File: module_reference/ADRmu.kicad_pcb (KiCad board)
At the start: 4 copper layers, 160 x 100 mm, 139 parts, among them J101 Harting 09042326831, J102 10Vf, J103 10Vs, J104 7Vref, J105 Lo, J301 Conn_01x01, J302 Conn_01x01, J303 Conn_01x01, J304 Conn_01x01, J305 Conn_01x01, Q201 BD135, Q301 MMBT3904, U201 ADR1000, U202 OPA2140, U203 ADA4523-1, U301 L78L33_SOT89, U302 LT3439, U303 TMP117, U304 BR24H64FVM, U305 LT3045xMSE

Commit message: Lowered Vreg to 11V to keep things cooler
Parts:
- R311: value 120k -> 110k
- R312: value 1M8 -> 1M
- R313: value 49k9 -> 30k
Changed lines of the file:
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@@
       (effects (font (size 1 1) (thickness 0.15)))
     )
-    (fp_text value "1M8" (at 0 1.65) (layer "F.Fab")
+    (fp_text value "1M" (at 0 1.65) (layer "F.Fab")
       (effects (font (size 1 1) (thickness 0.15)))
     )
@@
       (effects (font (size 1 1) (thickness 0.15)))
     )
-    (fp_text value "120k" (at 0 1.65) (layer "F.Fab")
+    (fp_text value "110k" (at 0 1.65) (layer "F.Fab")
       (effects (font (size 1 1) (thickness 0.15)))
     )
@@
       (effects (font (size 1 1) (thickness 0.15)))
     )
-    (fp_text value "49k9" (at 0 1.65) (layer "F.Fab")
+    (fp_text value "30k" (at 0 1.65) (layer "F.Fab")
       (effects (font (size 1 1) (thickness 0.15)))
     )

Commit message: Rev 0.5 routed
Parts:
- removed the JP210 at (142.1, 110.0)
- removed the JP211 at (149.0, 91.8)
- removed the JP212 at (142.1, 102.4)
- removed the JP213 at (155.2, 110.9)
- removed the JP215 at (142.1, 94.8)
- removed the JP219 at (142.1, 112.7)
- removed the JP222 at (83.0, 113.8)
- removed JP225: Jumper_2_Open, Jumper:SolderJumper-2_P1.3mm_Open_RoundedPad1.0x1.5mm
- added J201: Conn_01x01, Connector_Wire:SolderWire-0.1sqmm_1x01_D0.4mm_OD1mm, F.Cu at (97.8, 96.5)
- added J202: Conn_01x01, Connector_Wire:SolderWire-0.1sqmm_1x01_D0.4mm_OD1mm, F.Cu at (95.2, 99.1)
- added J203: Conn_01x01, Connector_Wire:SolderWire-0.1sqmm_1x01_D0.4mm_OD1mm, F.Cu at (99.0, 113.0)
- added J204: Conn_01x01, Connector_Wire:SolderWire-0.1sqmm_1x01_D0.4mm_OD1mm, F.Cu at (95.2, 94.0)
- added J205: Conn_01x01, Connector_Wire:SolderWire-0.1sqmm_1x01_D0.4mm_OD1mm, F.Cu at (95.2, 96.5)
- added J206: Conn_01x01, Connector_Wire:SolderWire-0.1sqmm_1x01_D0.4mm_OD1mm, F.Cu at (97.8, 99.1)
- added J207: Conn_01x01, Connector_Wire:SolderWire-0.1sqmm_1x01_D0.4mm_OD1mm, F.Cu at (97.8, 101.6)
- added J208: Conn_01x01, Connector_Wire:SolderWire-0.1sqmm_1x01_D0.4mm_OD1mm, F.Cu at (97.8, 104.1)
- added JP214: Jumper_2_Open, Jumper:SolderJumper-2_P1.3mm_Open_RoundedPad1.0x1.5mm, F.Cu at (142.7, 115.3)
- added JP218: Jumper_2_Bridged, Jumper:SolderJumper-2_P1.3mm_Bridged_RoundedPad1.0x1.5mm, F.Cu at (82.2, 113.8)
- added JP220: Jumper_2_Bridged, Jumper:SolderJumper-2_P1.3mm_Bridged_RoundedPad1.0x1.5mm, B.Cu at (83.2, 98.2)
- added R218: 30k, Resistor_SMD:R_0805_2012Metric, F.Cu at (87.5, 117.2)
- added R222: DNP, Resistor_SMD:R_0805_2012Metric, F.Cu at (80.0, 129.2)
- added R223: DNP, Crystal:Crystal_HC52-U_Vertical, F.Cu at (80.0, 127.3)
- added R224: DNP, Resistor_SMD:R_0805_2012Metric, F.Cu at (80.0, 120.0)
- added R225: DNP, Crystal:Crystal_HC52-U_Vertical, F.Cu at (80.0, 121.9)
- JP201: value Jumper_2_Bridged -> Jumper_2_Open; footprint Jumper:SolderJumper-2_P1.3mm_Bridged_RoundedPad1.0x1.5mm -> Jumper:SolderJumper-2_P1.3mm_Open_RoundedPad1.0x1.5mm
- R201: footprint Crystal:Crystal_HC52-U_Vertical -> Resistor_SMD:R_0805_2012Metric
- R202: footprint Resistor_SMD:R_0805_2012Metric -> Crystal:Crystal_HC52-U_Vertical
- R221: renamed from R218; value 0 -> DNP
- R226: renamed from R220; value 0 -> DNP
- moved R202 14.8 mm to (93.0, 113.0), turned to 0 degrees
- moved JP201 13.6 mm to (94.8, 113.0), turned to 180 degrees
- moved R201 12.1 mm to (94.8, 113.0), turned to 0 degrees
- moved JP215 2.25 mm to (141.1, 118.4)
- moved JP207 2.08 mm to (101.0, 121.9)
- moved R210 2.08 mm to (101.0, 121.9)
- moved R211 2.08 mm to (102.9, 121.9)
- moved R216 1.84 mm to (102.2, 117.0)
- moved R217 1.84 mm to (104.2, 117.0)
- moved R221 1.57 mm to (147.5, 117.9)
- moved R226 1.57 mm to (149.4, 117.9)
- moved RN201 1.14 mm to (92.7, 91.4)
- moved JP212 0.92 mm to (142.2, 96.5), turned to 90 degrees
- moved R204 0.35 mm to (89.8, 132.8)
- moved RN202 0.27 mm to (145.0, 94.5)
- renumbered JP205 to JP204, JP206 to JP205, JP208 to JP206, JP209 to JP207, JP214 to JP208, JP216 to JP209, JP217 to JP210, JP218 to JP211, JP207 to JP212, JP221 to JP213, JP220 to JP215, JP223 to JP216, JP224 to JP217, JP226 to JP219, JP227 to JP221, JP228 to JP222, R221 to R220, R222 to R227, R223 to R228, R224 to R229, R225 to R230, R226 to R231, R227 to R232
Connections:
- net /DC-DC/U303_a0 renamed /DC-DC/U304_a0
- net /DC-DC/U303_a1 renamed /DC-DC/U304_a1
- net /DC-DC/U303_a2 renamed /DC-DC/U304_a2
- net /DC-DC/U304_add0 renamed /DC-DC/U303_add0
- net /DC-DC/U304_alert renamed /DC-DC/U303_alert
- net /DC-DC/filtered+ renamed /DC-DC/rectified+
- net /ref/JP221_Pin2 renamed /ref/JP214_Pin2
- C205 pad 2: /ref/ADR_Pin4 -> /ref/U202A_-in
- JP201 pad 1: /ref/ADR_Pin7 -> /ref/JP201_Pin1
- JP201 pad 2: /ref/RN201_Pin15 -> /ref/ADR_Pin6
- JP212 pad 1: /ref/10Vsense -> /ref/U203_-in
- JP212 pad 2: /ref/RN202_Pin2 -> /ref/RN212_Pin2
- JP215 pad 1: /ref/JP211_Pin1 -> /ref/ADR_Pin7
- R201 pad 1: /ref/ADR_Pin7 -> /ref/ADR_Pin6
- R201 pad 2: /ref/RN201_Pin15 -> /ref/JP201_Pin1
- R202 pad 1: /ref/ADR_Pin7 -> /ref/ADR_Pin6
- R202 pad 2: /ref/RN201_Pin15 -> /ref/JP201_Pin1
- R221 pad 2: /ref/RN202_Pin16 -> /ref/RN202_Pin9
- R226 pad 2: /ref/RN202_Pin16 -> /ref/RN202_Pin9
- RN201 pad 10: /ref/RN201_Pin10 -> /ref/ADR_Pin7
- RN201 pad 11: /ref/ADR_Pin7 -> /ref/RN201_Pin11
- RN201 pad 12: /ref/RN201_Pin10 -> /ref/RN201_Pin12
- RN201 pad 13: /ref/ADR_Pin7 -> /ref/RN201_Pin13
- RN201 pad 16: /ref/RN201_Pin14 -> /ref/RN201_Pin15
- RN201 pad 2: /ref/ADR_Pin6 -> /ref/RN201_Pin2
- RN201 pad 3: /ref/RN201_Pin5 -> /ref/RN201_Pin3
- RN201 pad 4: /ref/ADR_Pin6 -> /ref/RN201_Pin4
- RN201 pad 5: /ref/RN201_Pin5 -> /ref/ADR_Pin6
- RN202 pad 1: /ref/RN202_Pin1 -> /ref/RN212_Pin2
- RN202 pad 10: /ref/RN202_Pin14 -> /ref/10Vsense
- RN202 pad 11: /ref/RN202_Pin14 -> /ref/ADR_Pin7
- RN202 pad 12: /ref/ADR_Pin7 -> /ref/10Vsense
- RN202 pad 13: /ref/U203_-in -> /ref/10Vsense
- RN202 pad 14: /ref/RN202_Pin14 -> /ref/ADR_Pin7
- RN202 pad 15: /ref/RN202_Pin14 -> /ref/10Vsense
- RN202 pad 16: /ref/RN202_Pin16 -> /ref/10Vsense
- RN202 pad 2: /ref/RN202_Pin2 -> /ref/U203_-in
- RN202 pad 4: /ref/RN202_Pin5 -> /ref/U203_-in
- RN202 pad 5: /ref/RN202_Pin5 -> /ref/U203_-in
- RN202 pad 7: /ref/10Vsense -> /ref/U203_-in
- RN202 pad 8: /ref/RN202_Pin8 -> /ref/U203_-in
- RN202 pad 9: /ref/RN202_Pin16 -> /ref/RN202_Pin9
- U202 pad 2: /ref/ADR_Pin4 -> /ref/U202A_-in
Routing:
- net /ref/JP211_Pin1: track 45.6 -> 0.00 mm
- net /ref/U203_-in: track 42.9 -> 0.00 mm
- net /ref/ADR_Pin6: track 91.2 -> 59.6 mm, vias 0 -> 1
- net /ref/ADR_Pin4: track 93.1 -> 73.0 mm
- net /ref/U202A_-in: track 0.00 -> 18.6 mm
- net /ref/RN202_Pin14: track 15.9 -> 0.00 mm
- net /ref/RN204_Pin11: track 17.4 -> 3.42 mm
- net /ref/ADR_Pin5: track 69.8 -> 83.4 mm
- net /ref/RN202_Pin2: track 8.58 -> 0.00 mm
- net /ref/RN201_Pin5: track 7.57 -> 0.00 mm
- net /ref/ADR_Pin7: track 122.6 -> 115.1 mm, vias 1 -> 2
- net /ref/RN204_Pin16: track 9.80 -> 17.2 mm
- net /ref/RN201_Pin10: track 7.07 -> 0.00 mm
- net /ref/RN201_Pin15: track 9.45 -> 2.54 mm
- net /ref/RN202_Pin9: track 0.00 -> 6.29 mm
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- added copper zone on F.Cu, net /ref/ADR_Pin5
- removed copper zone on F.Cu, net /ref/RN202_Pin16
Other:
- board text added: "ADRmu 10V Standard Rev 0.5"
- board text removed: "ADRmu 10V Standard Rev 0.4"

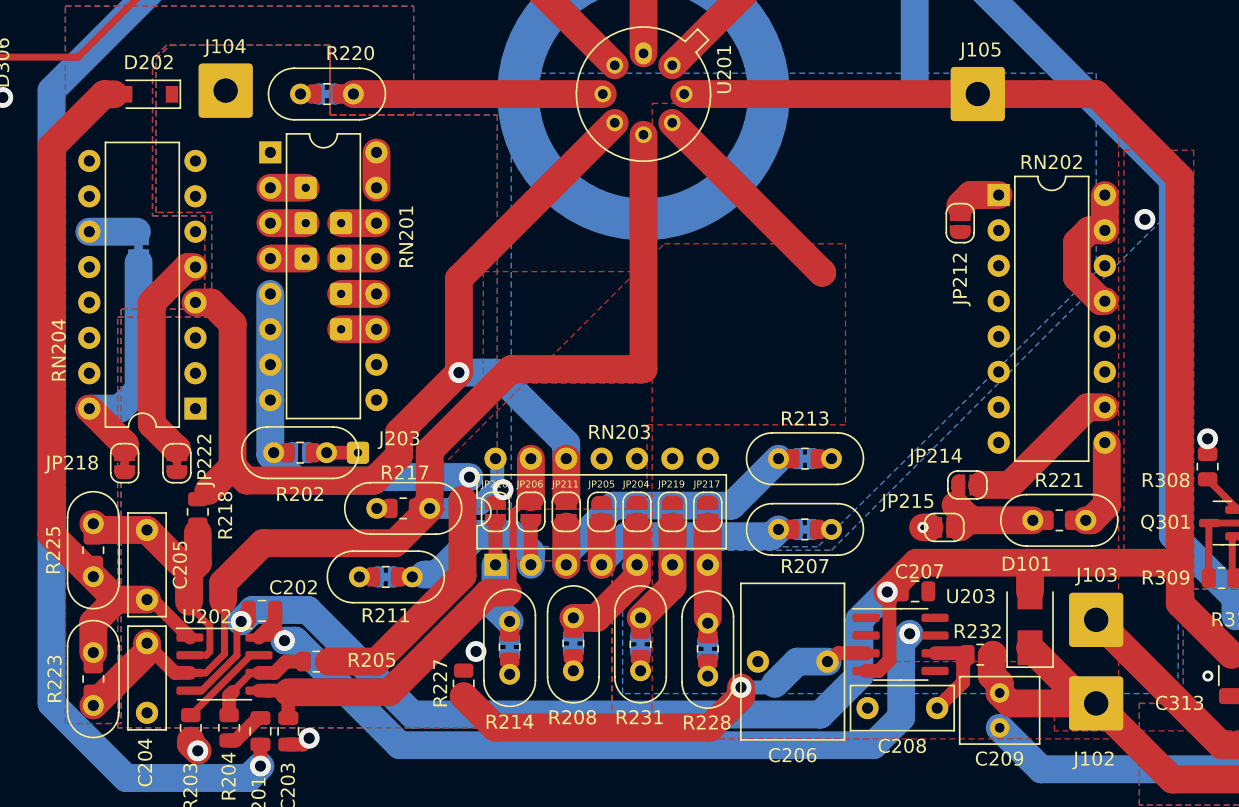
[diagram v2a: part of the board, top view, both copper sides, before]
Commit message: No longer configured for PRND by default
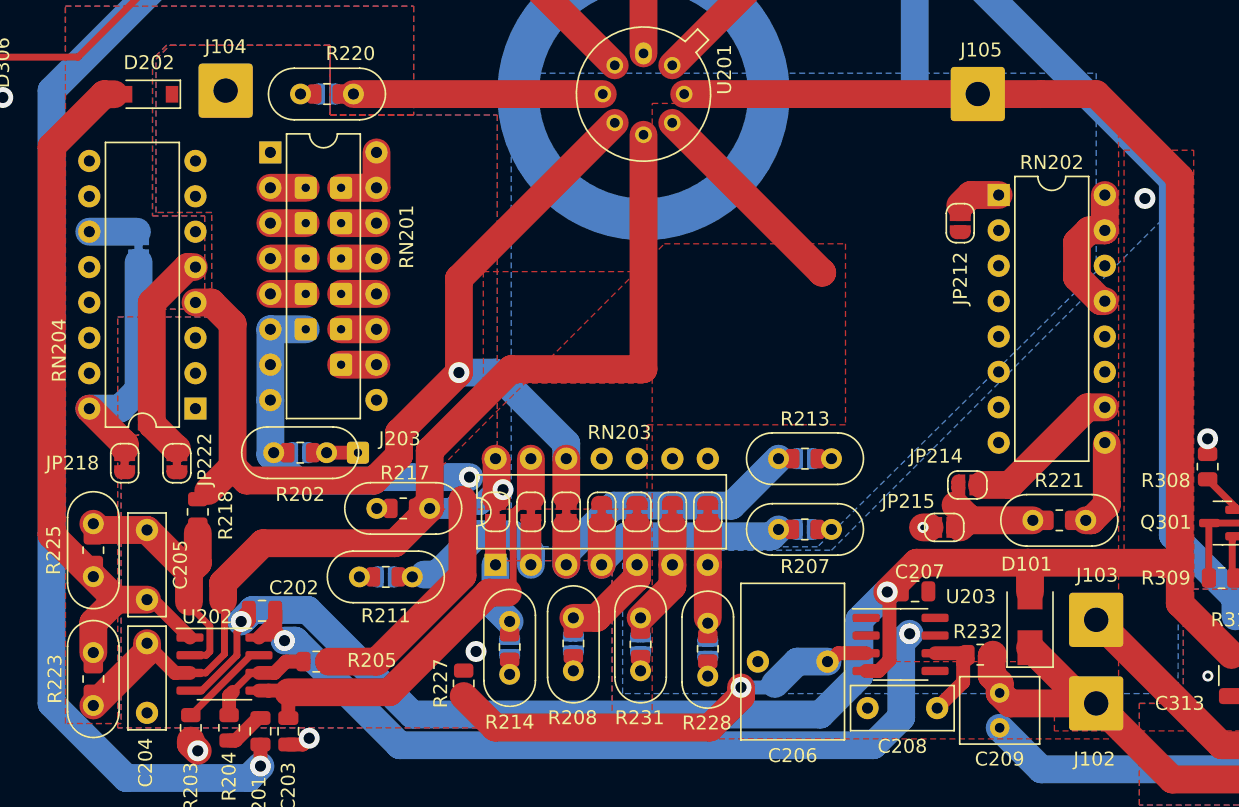
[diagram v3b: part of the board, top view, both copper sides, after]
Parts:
- added J209: Conn_01x01, Connector_Wire:SolderWire-0.1sqmm_1x01_D0.4mm_OD1mm, F.Cu at (97.8, 106.7)
- added J210: Conn_01x01, Connector_Wire:SolderWire-0.1sqmm_1x01_D0.4mm_OD1mm, F.Cu at (97.8, 94.0)
- added J211: Conn_01x01, Connector_Wire:SolderWire-0.1sqmm_1x01_D0.4mm_OD1mm, F.Cu at (95.2, 101.6)
- added J212: Conn_01x01, Connector_Wire:SolderWire-0.1sqmm_1x01_D0.4mm_OD1mm, F.Cu at (95.2, 104.1)
- JP202, JP203, JP207, JP208, JP209, JP213, JP216, JP221: value Jumper_2_Bridged -> Jumper_2_Open; footprint Jumper:SolderJumper-2_P1.3mm_Bridged_RoundedPad1.0x1.5mm -> Jumper:SolderJumper-2_P1.3mm_Open_RoundedPad1.0x1.5mm
- JP204, JP205, JP206, JP210, JP211, JP217, JP219: value Jumper_2_Open -> Jumper_2_Bridged; footprint Jumper:SolderJumper-2_P1.3mm_Open_RoundedPad1.0x1.5mm -> Jumper:SolderJumper-2_P1.3mm_Bridged_RoundedPad1.0x1.5mm
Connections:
- RN201 pad 5: /ref/ADR_Pin6 -> /ref/RN201_Pin5
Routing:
- net /ref/RN201_Pin5: track 0.00 -> 2.54 mm
- net /ref/RN201_Pin15: track 2.54 -> 5.08 mm
- net /ref/ADR_Pin7: track 115.1 -> 117.7 mm
- net /ref/ADR_Pin5: track 83.4 -> 85.8 mm

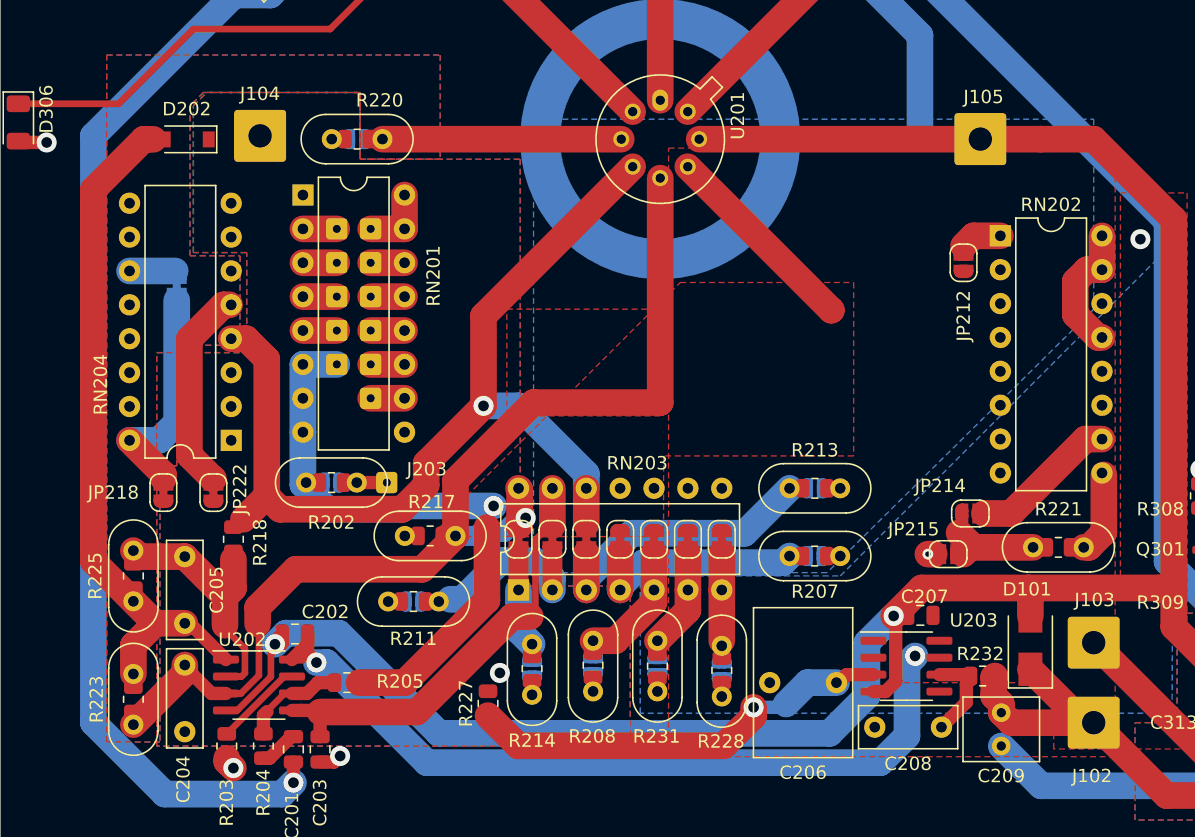
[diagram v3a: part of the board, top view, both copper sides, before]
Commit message: New backplane, Reference Rev 0.6 with heated resistor network support
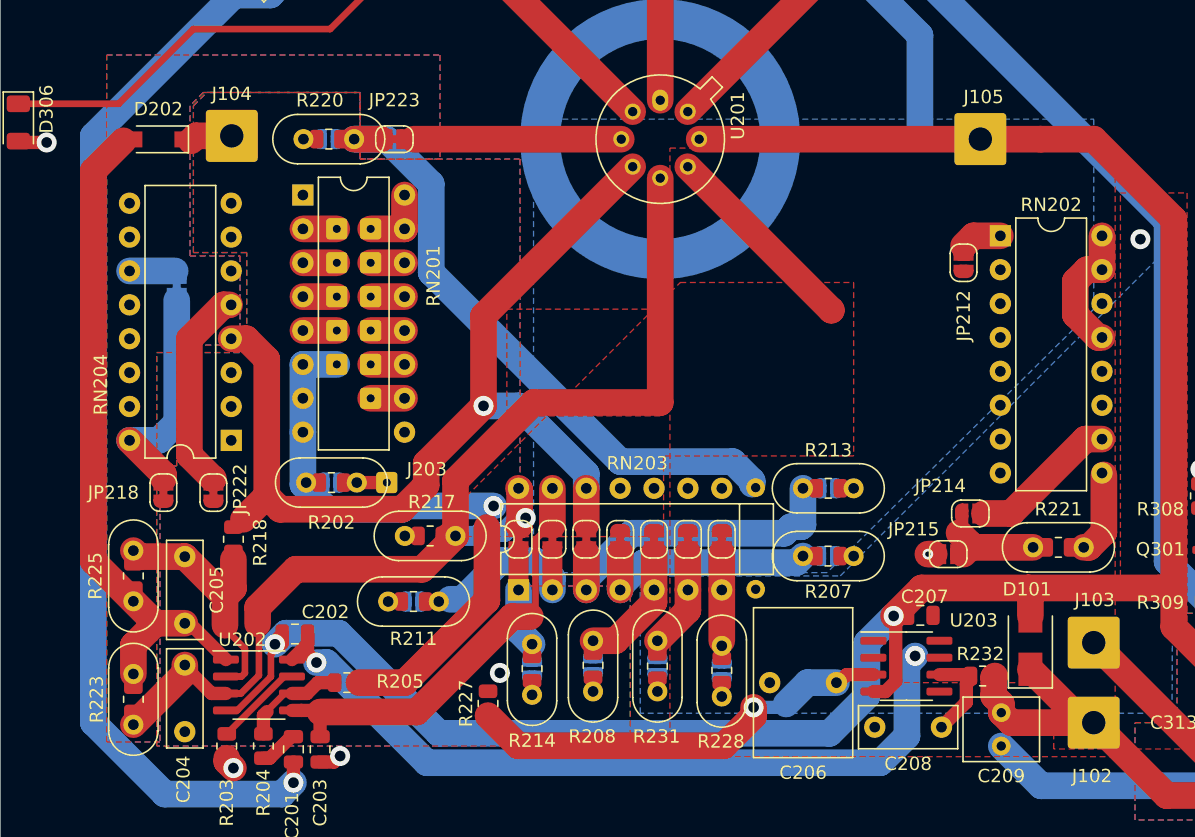
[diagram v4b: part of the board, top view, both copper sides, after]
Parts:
- added JP223: Jumper_2_Bridged, Jumper:SolderJumper-2_P1.3mm_Bridged_RoundedPad1.0x1.5mm, F.Cu at (99.6, 87.3)
- added R233: 0, Resistor_THT:R_Axial_DIN0204_L3.6mm_D1.6mm_P7.62mm_Horizontal, F.Cu at (126.7, 121.0)
- moved JP213 2.12 mm to (94.7, 87.2)
- moved R219 2.12 mm to (94.7, 87.2)
- moved D202 2.12 mm to (81.9, 87.3)
- moved J104 2.12 mm to (87.4, 87.0)
- moved R220 2.12 mm to (96.6, 87.2)
- moved JP203 1.01 mm to (132.1, 118.5)
- moved JP209 1.01 mm to (132.1, 113.4)
- moved R207 1.01 mm to (130.2, 118.5)
- moved R209 1.01 mm to (132.1, 118.5)
- moved R213 1.01 mm to (130.2, 113.4)
- moved R215 1.01 mm to (132.1, 113.4)
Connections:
- JP213 pad 1: /ref/ADR_Pin3 -> Net-(JP213-Pad1)
- R219 pad 1: /ref/ADR_Pin3 -> Net-(JP213-Pad1)
- R220 pad 1: /ref/ADR_Pin3 -> Net-(JP213-Pad1)
- RN203 pad 10: (no net) -> /ref/ADR_Pin6
- RN203 pad 8: (no net) -> /ref/U203_-in
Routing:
- net /ref/ADR_Pin3: track 20.1 -> 76.0 mm
- net Net-(JP213-Pad1): track 0.00 -> 48.8 mm
- net /ref/7Vref: track 0.00 -> 3.20 mm
- net /ref/RN203_Pin3: track 23.9 -> 26.5 mm
- net /ref/U202A_out: track 51.4 -> 49.9 mm
- net /ref/RN203_Pin4: track 18.9 -> 19.9 mm
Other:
- board text added: "ADRmu 10V Standard Rev 0.6"
- board text removed: "ADRmu 10V Standard Rev 0.5"
